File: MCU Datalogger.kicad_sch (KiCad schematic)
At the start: 25 parts, among them U1 24LC1025, U2 24LC1025, U3 ATMEGA328P-AU, U4 DS1337S_, Y1 Crystal, Y2 Crystal

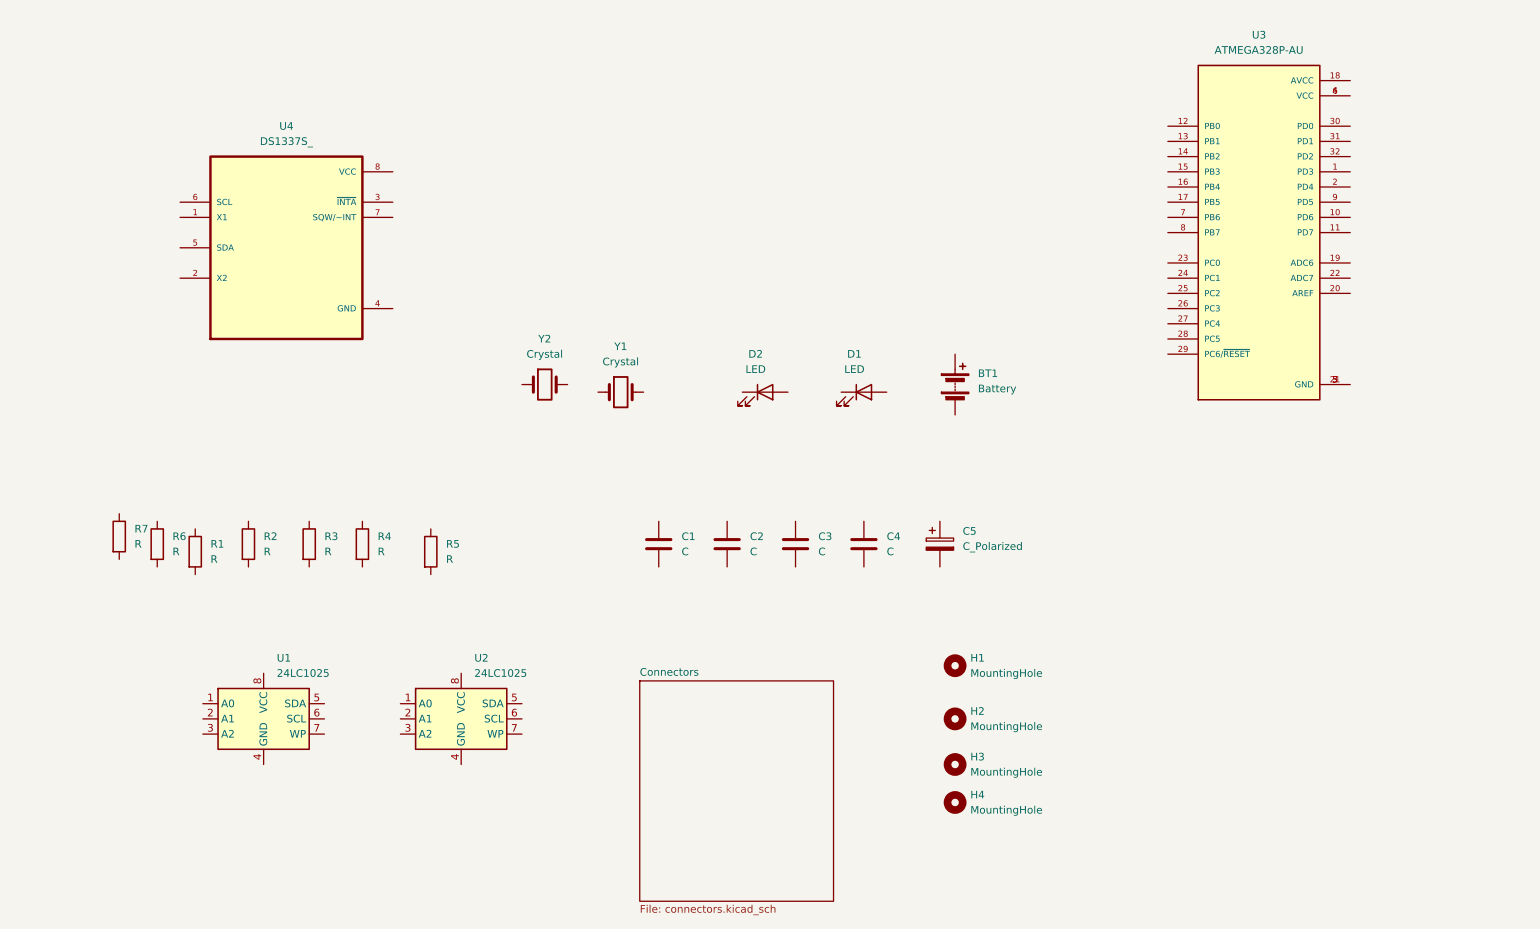
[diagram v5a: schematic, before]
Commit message: Arranged symbols.
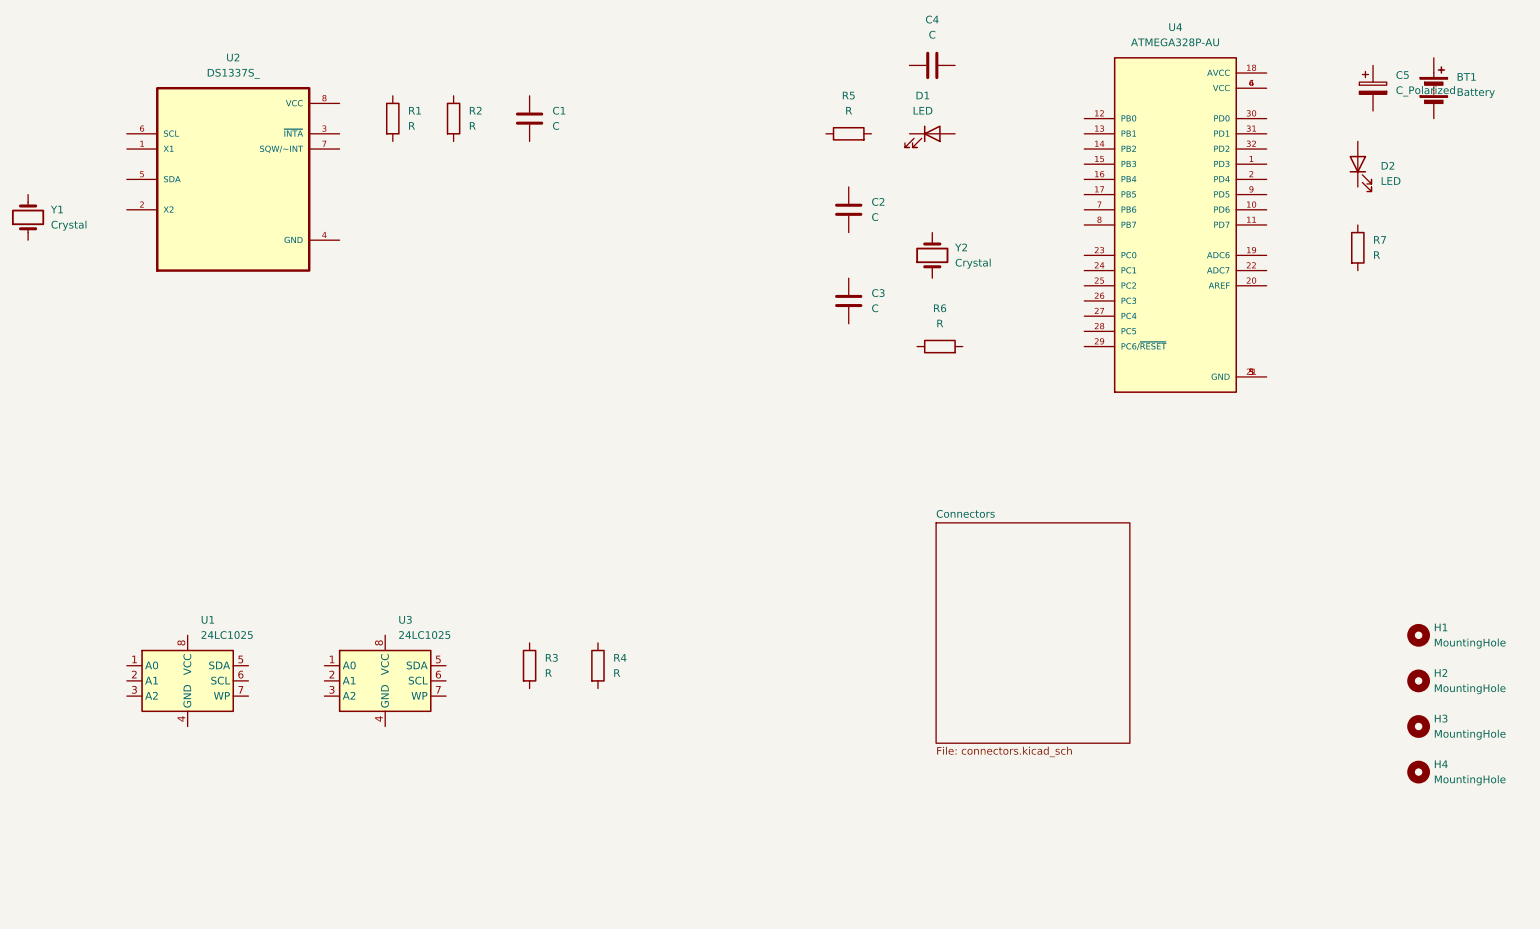
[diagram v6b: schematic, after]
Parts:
- renumbered C2 to C1, C4 to C2, C1 to C4, D2 to D1, D1 to D2, R3 to R1, R1 to R3, R6 to R4, R4 to R5, R7 to R6, R5 to R7, U4 to U2, U2 to U3, U3 to U4, Y2 to Y1, Y1 to Y2
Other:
- moved on the sheet: BT1, C1, C2, C3, C4, C5, D1, D2, H1, H2, H3, H4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

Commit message: Added component values.
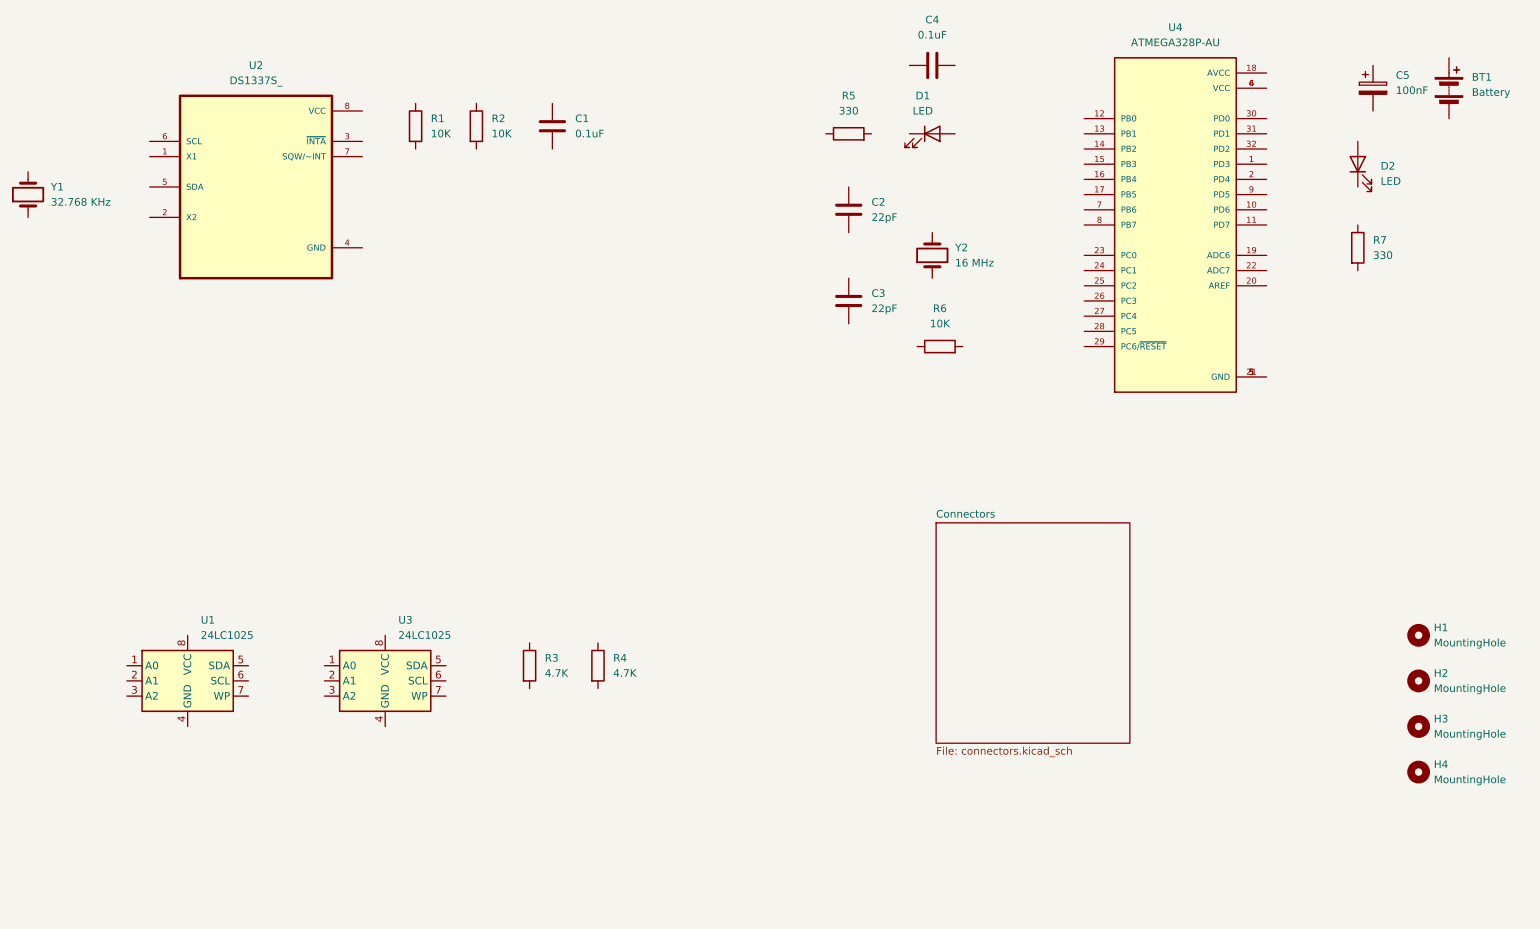
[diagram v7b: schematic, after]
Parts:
- C1, C4: value C -> 0.1uF
- C2, C3: value C -> 22pF
- C5: value C_Polarized -> 100nF
- R1, R2, R6: value R -> 10K
- R3, R4: value R -> 4.7K
- R5, R7: value R -> 330
- Y1: value Crystal -> 32.768 KHz
- Y2: value Crystal -> 16 MHz
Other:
- moved on the sheet: BT1, C1, R1, R2, U2, Y1

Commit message: Completed symbol-footprint associations.
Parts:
- BT1: footprint (none) -> Connector_PinHeader_2.54mm:PinHeader_1x02_P2.54mm_Vertical
- C1, C2, C3, C4, C5: footprint (none) -> Capacitor_SMD:C_0805_2012Metric
- D1, D2: footprint (none) -> LED_SMD:LED_0805_2012Metric
- H1, H2, H3, H4: footprint (none) -> MountingHole:MountingHole_2.1mm
- R1, R2, R3, R4, R5, R6, R7: footprint (none) -> Resistor_SMD:R_0805_2012Metric
- U1, U3: footprint (none) -> Package_SO:SOIC-8_5.23x5.23mm_P1.27mm
- U2: footprint DS1337S_:SOIC127P600X175-8N -> Footprints:SOIC127P600X175-8N
- U4: footprint ATMEGA328P-AU:QFP80P900X900X120-32N -> Footprints:QFP80P900X900X120-32N
- Y1, Y2: footprint (none) -> Crystal:Crystal_SMD_5032-2Pin_5.0x3.2mm_HandSoldering
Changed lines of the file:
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@@
 			)
 		)
-		(property "Footprint" ""
+		(property "Footprint" "Crystal:Crystal_SMD_5032-2Pin_5.0x3.2mm_HandSoldering"
 			(at 25.4 59.69 0)
 			(effects
@@
 			)
 		)
-		(property "Footprint" ""
+		(property "Footprint" "Capacitor_SMD:C_0805_2012Metric"
 			(at 251.1552 45.72 0)
 			(effects
@@
 			)
 		)
-		(property "Footprint" ""
+		(property "Footprint" "Resistor_SMD:R_0805_2012Metric"
 			(at 88.392 48.26 90)
 			(effects
@@
 			)
 		)
-		(property "Footprint" ""
+		(property "Footprint" "Resistor_SMD:R_0805_2012Metric"
 			(at 245.872 68.58 90)
 			(effects
@@
 			)
 		)
-		(property "Footprint" ""
+		(property "Footprint" "Resistor_SMD:R_0805_2012Metric"
 			(at 177.8 86.868 90)
 			(effects
@@
 			)
 		)
-		(property "Footprint" ""
+		(property "Footprint" "MountingHole:MountingHole_2.1mm"
 			(at 257.81 140.97 0)
 			(effects
@@
 			)
 		)
-		(property "Footprint" ""
+		(property "Footprint" "MountingHole:MountingHole_2.1mm"
 			(at 257.81 148.59 0)
 			(effects
@@
 			)
 		)
-		(property "Footprint" ""
+		(property "Footprint" "LED_SMD:LED_0805_2012Metric"
 			(at 247.65 54.61 0)
 			(effects
@@
 			)
 		)
-		(property "Footprint" ""
+		(property "Footprint" "MountingHole:MountingHole_2.1mm"
 			(at 257.81 133.35 0)
 			(effects
@@
 			)
 		)
-		(property "Footprint" ""
+		(property "Footprint" "Capacitor_SMD:C_0805_2012Metric"
 			(at 163.5252 81.28 0)
 			(effects
@@
 			)
 		)
-		(property "Footprint" ""
+		(property "Footprint" "Capacitor_SMD:C_0805_2012Metric"
 			(at 163.5252 66.04 0)
 			(effects
@@
 			)
 		)
-		(property "Footprint" "DS1337S_:SOIC127P600X175-8N"
+		(property "Footprint" "Footprints:SOIC127P600X175-8N"
 			(at 63.5 58.42 0)
 			(effects
@@
 			)
 		)
-		(property "Footprint" ""
+		(property "Footprint" "Capacitor_SMD:C_0805_2012Metric"
 			(at 180.34 37.1348 0)
 			(effects
@@
 			)
 		)
-		(property "Footprint" ""
+		(property "Footprint" "Crystal:Crystal_SMD_5032-2Pin_5.0x3.2mm_HandSoldering"
 			(at 176.53 69.85 0)
 			(effects
@@
 			)
 		)
-		(property "Footprint" ""
+		(property "Footprint" "Capacitor_SMD:C_0805_2012Metric"
 			(at 113.9952 52.07 0)
 			(effects
@@
 			)
 		)
-		(property "Footprint" ""
+		(property "Footprint" "Package_SO:SOIC-8_5.23x5.23mm_P1.27mm"
 			(at 85.09 140.97 0)
 			(effects
@@
 			)
 		)
-		(property "Footprint" "ATMEGA328P-AU:QFP80P900X900X120-32N"
+		(property "Footprint" "Footprints:QFP80P900X900X120-32N"
 			(at 217.17 64.77 0)
 			(effects
@@
 			)
 		)
-		(property "Footprint" ""
+		(property "Footprint" "Connector_PinHeader_2.54mm:PinHeader_1x02_P2.54mm_Vertical"
 			(at 262.89 40.386 90)
 			(effects
@@
 			)
 		)
-		(property "Footprint" ""
+		(property "Footprint" "Package_SO:SOIC-8_5.23x5.23mm_P1.27mm"
 			(at 52.07 140.97 0)
 			(effects
@@
 			)
 		)
-		(property "Footprint" ""
+		(property "Footprint" "Resistor_SMD:R_0805_2012Metric"
 			(at 98.552 48.26 90)
 			(effects
@@
 			)
 		)
-		(property "Footprint" ""
+		(property "Footprint" "MountingHole:MountingHole_2.1mm"
 			(at 257.81 156.21 0)
 			(effects
@@
 			)
 		)
-		(property "Footprint" ""
+		(property "Footprint" "Resistor_SMD:R_0805_2012Metric"
 			(at 162.56 51.308 90)
 			(effects
@@
 			)
 		)
-		(property "Footprint" ""
+		(property "Footprint" "LED_SMD:LED_0805_2012Metric"
 			(at 176.53 49.53 0)
 			(effects
@@
 			)
 		)
-		(property "Footprint" ""
+		(property "Footprint" "Resistor_SMD:R_0805_2012Metric"
 			(at 118.872 138.43 90)
 			(effects
@@
 			)
 		)
-		(property "Footprint" ""
+		(property "Footprint" "Resistor_SMD:R_0805_2012Metric"
 			(at 107.442 138.43 90)
 			(effects
